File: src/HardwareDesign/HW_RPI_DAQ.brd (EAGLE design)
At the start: 180 x 100 mm, 348 parts, among them IC10 ADS9234RIRHBR, IC11 MCP6001RT, IC12 MCP1525T-I/TT, IC13 MCP6001RT, IC14 TPS65131, IC15 TPS7A39, IC16 SN74LVC2G66, IC17 74LVC1G04, IC2 AP22653W6, IC22 DAC8568, IC23 MCP6001RT, IC24 MCP6001RT, IC25 MCP6001RT, IC26 MCP6001RT, IC27 MCP6001RT, IC28 MCP6001RT, IC29 MCP6001RT, IC3 74LVC1G07, IC30 MCP6001RT, IC31 MCP6001RT, IC32 LSF0108, IC33 LSF0108, IC34 LSF0108, IC35 LSF0108, IC36 MCP23S18, IC38 SN74LVC2G66, IC39 74LVC1G04, IC4 RT9742NGV, IC6 DG409, IC7 ADA4254ACPZ, IC8 DG409, IC9 ADA4254ACPZ, J1 10164227-1001A1RLF, J2 10164227-1001A1RLF, J7 2-5174225-5, SW1 1825027-8, T2 IRLML5203, X2 CRYSTAL

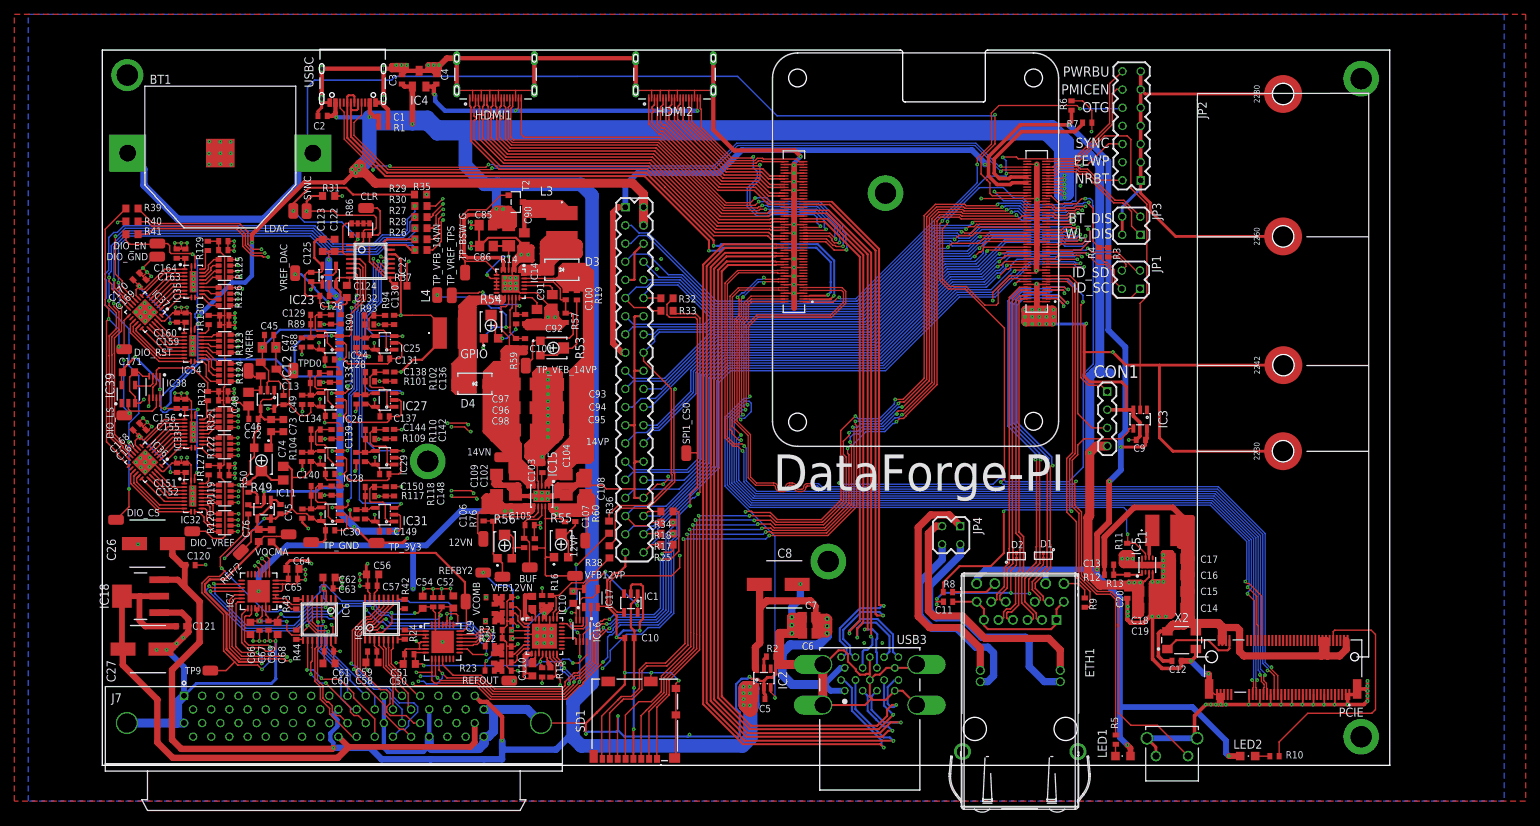
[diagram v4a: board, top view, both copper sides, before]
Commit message: update schematics with new testpoints
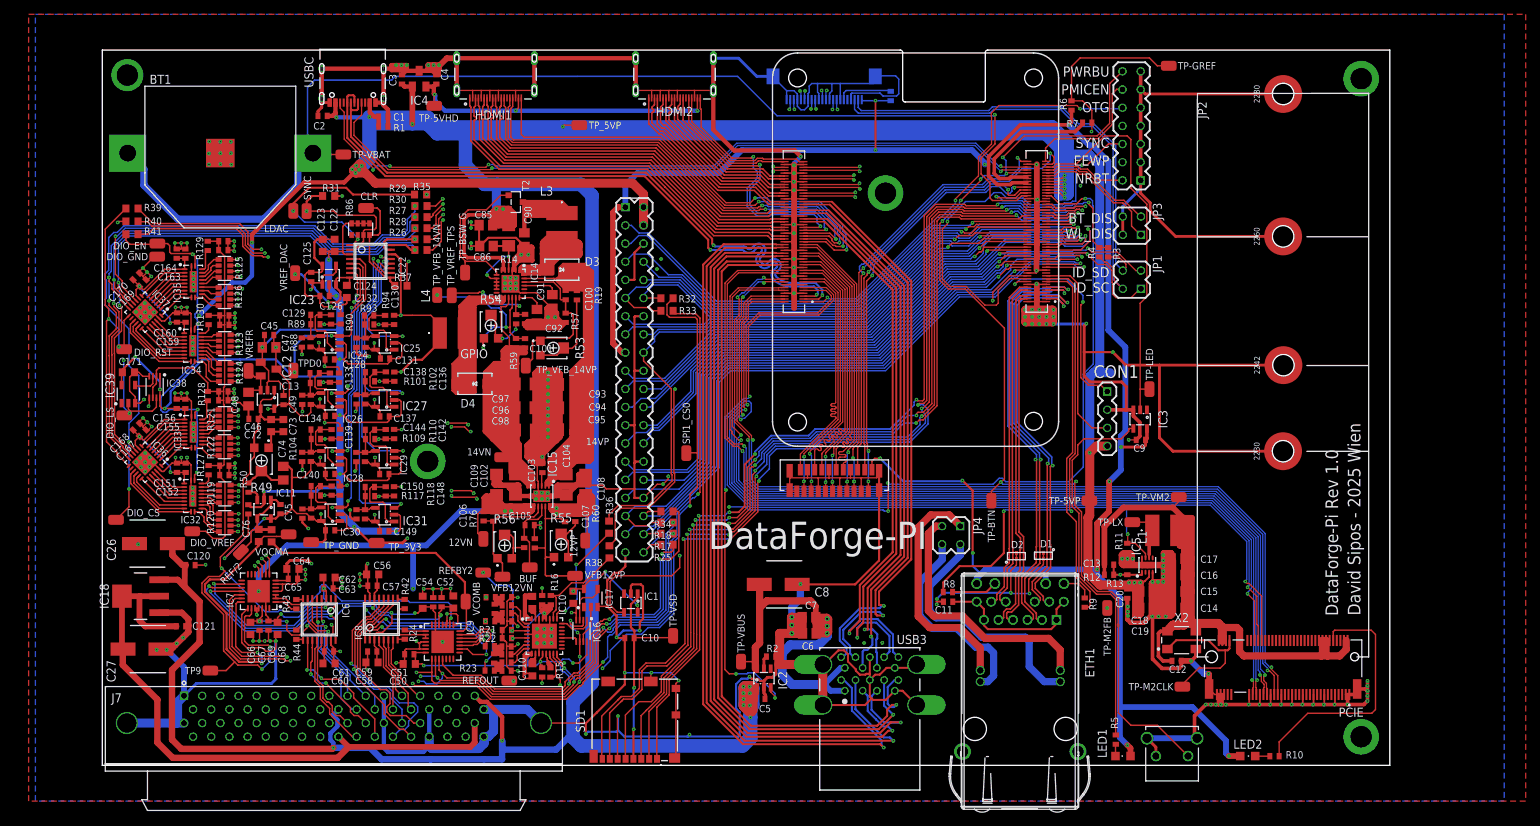
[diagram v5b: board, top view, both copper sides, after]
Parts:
- added J3: FH12-22S-0.5SVA, ds_con:FH12-22S-0.5SH
- added J4: FH12-22S-0.5SH(55), ds_con:CONN_FH12-22S-0.5SH(55)_HIR
- added R61: 2.2K 1%, ds_passive:0402
- added TP-5VHD, TP-5VP, TP-BTN, TP-GREF, TP-LED, TP-LX, TP-M2CLK, TP-M2FB, TP-VBAT, TP-VBUS, TP-VM2, TP-VSD, TP_5VP: TP, ds_passive:TP
- moved JP1 0.12 mm to (118.9, 67.9)
- moved JP3 0.08 mm to (118.9, 75.5)
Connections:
- new net N$45: J4.17, R61.1
- net +3V3: now also J3.22, J4.22, R61.2
- net +5V: now also TP-5VP.TP, TP_5VP.TP
- net CAM_GPIO0: now also J3.17
- net CAM_GPIO1: now also J3.18
- net DPHY0_C_N: now also J3.8
- net DPHY0_C_P: now also J3.9
- net DPHY0_D0_N: now also J3.2
- net DPHY0_D0_P: now also J3.3
- net DPHY0_D1_N: now also J3.5
- net DPHY0_D1_P: now also J3.6
- net DPHY0_D2_N: now also J3.11
- net DPHY0_D2_P: now also J3.12
- net DPHY0_D3_N: now also J3.14
- net DPHY0_D3_P: now also J3.15
- net DPHY1_C_N: now also J4.8
- net DPHY1_C_P: now also J4.9
- net DPHY1_D0_N: now also J4.2
- net DPHY1_D0_P: now also J4.3
- net DPHY1_D1_N: now also J4.5
- net DPHY1_D1_P: now also J4.6
- net DPHY1_D2_N: now also J4.11
- net DPHY1_D2_P: now also J4.12
- net DPHY1_D3_N: now also J4.14
- net DPHY1_D3_P: now also J4.15
- net GND: now also J3.1, J3.10, J3.13, J3.16, J3.19, J3.23, J3.24, J3.25, J3.26, J3.4, J3.7, J4.1, J4.10, J4.13, J4.16, J4.19, J4.23, J4.24, J4.4, J4.7
- net GPIO_VREF: now also TP-GREF.TP
- net HDMI_5V: now also TP-5VHD.TP
- net M2_3V3: now also TP-VM2.TP
- net N$10: now also TP-M2FB.TP
- net N$11: now also TP-M2CLK.TP
- net N$9: now also TP-LX.TP
- net NPWR_LED: now also TP-LED.TP
- net PWR_BUT: now also TP-BTN.TP
- net SCL0: now also J3.20
- net SCL1: now also J4.20
- net SDA0: now also J3.21
- net SDA1: now also J4.21
- net SD_PWR: now also TP-VSD.TP
- net VBAT: now also TP-VBAT.TP
- net VBUS: now also TP-VBUS.TP
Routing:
- net GND: track 2082.3 -> 2181.6 mm, vias 291 -> 288
- net CAM_GPIO0: track 0.00 -> 67.9 mm, vias 0 -> 4
- net SCL1: track 5.96 -> 66.5 mm
- net CAM_GPIO1: track 0.00 -> 60.2 mm, vias 0 -> 2
- net SDA0: track 0.00 -> 59.4 mm, vias 0 -> 4
- net SDA1: track 4.04 -> 61.6 mm
- net SCL0: track 0.00 -> 57.1 mm, vias 0 -> 2
- net +3V3: track 752.7 -> 793.3 mm, vias 32 -> 37
- net DPHY0_D3_P: track 0.00 -> 39.2 mm, vias 0 -> 2
- net DPHY0_D3_N: track 0.00 -> 38.9 mm
- net DPHY0_D2_N: track 0.00 -> 37.9 mm, vias 0 -> 2
- net DPHY0_D2_P: track 0.00 -> 37.5 mm
- net DPHY0_C_P: track 0.00 -> 37.3 mm, vias 0 -> 2
- net DPHY0_C_N: track 0.00 -> 36.9 mm
- net DPHY0_D1_N: track 0.00 -> 36.1 mm, vias 0 -> 2
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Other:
- board text added: "DataForge-Pi Rev 1.0"
- board text added: "David Sipos - 2025 Wien"

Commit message: update PDF schematics
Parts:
- IC1: value (none) -> RT9742GGJ
- IC5: value (none) -> AP3441SHE-7B
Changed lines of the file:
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@@
 <drawing>
 <settings>
-<setting alwaysvectorfont="yes"/>
+<setting alwaysvectorfont="no"/>
 <setting verticaltext="up"/>
 </settings>
@@
 <attribute name="NAME" x="50.365" y="17.335" size="1.016" layer="25"/>
 </element>
-<element name="IC1" library="ds_ic_peripherals" package="SOT23-5" package3d_urn="urn:adsk.eagle:package:25419215/2" value="" x="48.9" y="22.7" smashed="yes" rot="R180">
+<element name="IC1" library="ds_ic_peripherals" package="SOT23-5" package3d_urn="urn:adsk.eagle:package:25419215/2" value="RT9742GGJ" x="48.9" y="22.7" smashed="yes" rot="R180">
 <attribute name="NAME" x="50.73" y="23.14" size="1.016" layer="25"/>
 </element>
@@
 <attribute name="NAME" x="124.115" y="12.935" size="1.016" layer="25"/>
 </element>
-<element name="IC5" library="ds_ic_vreg" package="SON50P201X201X56-9T90X170N" package3d_urn="urn:adsk.eagle:package:46646832/1" value="" x="121.1" y="28" smashed="yes" rot="R90">
+<element name="IC5" library="ds_ic_vreg" package="SON50P201X201X56-9T90X170N" package3d_urn="urn:adsk.eagle:package:46646832/1" value="AP3441SHE-7B" x="121.1" y="28" smashed="yes" rot="R90">
 <attribute name="NAME" x="120.176" y="30.65" size="1.27" layer="25" rot="R90" align="bottom-center"/>
 <attribute name="VALUE" x="122.899" y="28" size="1.27" layer="27" rot="R90" align="top-center"/>
